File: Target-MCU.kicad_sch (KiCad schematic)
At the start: 19 parts, among them Q6 DMG1012UW-7, SW5 16V 50mA, U4 CH32V003F4P6

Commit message: Update parts
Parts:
- removed SW5: 16V 50mA, Tiny_Scarab:SW_Tactile_SPST_NO_Straight_ALPSALPINE_SKRP, symbol Tiny_Scarab:SW_SKRPASE010
- added SW5: 12V 50mA, Tiny_Scarab:SW_Tactile_SPST_NO_Straight_Korean-Hroparts_K2-1109SP-I4SA-04, symbol Tiny_Scarab:SW_K2-1109SP-I4SA-04
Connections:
- net GND: now also SW5.3, SW5.4
- net at C41.1, R25.2, R26.1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: now also SW5.1, SW5.2
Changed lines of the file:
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@@
     (effects (font (size 1.27 1.27)) (justify right))
-  )
-  (symbol (lib_id "Tiny_Scarab:SW_SKRPASE010") (at 191.77 54.61 270) (unit 1)
-    (in_bom yes) (on_board yes) (dnp no)
-    (property "Reference" "SW5" (at 193.04 53.34 90)
-      (effects (font (size 1.27 1.27)) (justify left))
-    )
-    (property "Value" "16V 50mA" (at 217.17 54.61 0)
-      (effects (font (size 1.27 1.27)) hide)
-    )
-    (property "Footprint" "Tiny_Scarab:SW_Tactile_SPST_NO_Straight_ALPSALPINE_SKRP" (at 219.71 54.61 0)
-      (effects (font (size 1.27 1.27)) hide)
-    )
-    (property "Datasheet" "https://www.farnell.com/datasheets/2864500.pdf" (at 214.63 54.61 0)
-      (effects (font (size 1.27 1.27)) hide)
-    )
-    (property "Manufacturer" "ALPSALPINE" (at 212.09 54.61 0)
-      (effects (font (size 1.27 1.27)) hide)
-    )
-    (property "MPN" "SKRPASE010" (at 209.55 54.61 0)
-      (effects (font (size 1.27 1.27)) hide)
-    )
-    (property "JLCPCB Part #" "C470427" (at 207.01 54.61 0)
-      (effects (font (size 1.27 1.27)) hide)
-    )
-    (property "DigiKey" "4809-SKRPADE010TR-ND" (at 204.47 54.61 0)
-      (effects (font (size 1.27 1.27)) hide)
-    )
-    (property "Farnell" "3261826" (at 201.93 54.61 0)
-      (effects (font (size 1.27 1.27)) hide)
-    )
-    (property "Mouser" "688-SKRPASE010" (at 199.39 54.61 0)
-      (effects (font (size 1.27 1.27)) hide)
-    )
-    (pin "4")
-    (pin "3")
-    (pin "2")
-    (pin "1")
-    (instances
-      (project "tiny-scarab"
-        (path "/156c5422-ee07-49a4-8263-a2dbd26b90bd/d0c4b0c3-1e7e-4a4c-add3-8d4a3a10843d"
-          (reference "SW5") (unit 1)
-        )
-      )
-    )
   )
   (symbol (lib_id "Tiny_Scarab:IC_CH32V003F4P6") (at 118.11 57.15 0) (unit 1)
@@
         )
       )
+    )
+  )
+  (symbol (lib_id "Tiny_Scarab:SW_K2-1109SP-I4SA-04") (at 191.77 54.61 270) (unit 1)
+    (in_bom yes) (on_board yes) (dnp no)
+    (property "Reference" "SW5" (at 193.04 53.34 90)
+      (effects (font (size 1.27 1.27)) (justify left))
+    )
+    (property "Value" "12V 50mA" (at 217.17 54.61 0)
+      (effects (font (size 1.27 1.27)) hide)
+    )
+    (property "Footprint" "Tiny_Scarab:SW_Tactile_SPST_NO_Straight_Korean-Hroparts_K2-1109SP-I4SA-04" (at 219.71 54.61 0)
+      (effects (font (size 1.27 1.27)) hide)
+    )
+    (property "Datasheet" "" (at 214.63 54.61 0)
+      (effects (font (size 1.27 1.27)) hide)
+    )
+    (property "Manufacturer" "Korean Hroparts Elec" (at 212.09 54.61 0)
+      (effects (font (size 1.27 1.27)) hide)
+    )
+    (property "MPN" "K2-1109SP-I4SA-04" (at 209.55 54.61 0)
+      (effects (font (size 1.27 1.27)) hide)
+    )
+    (property "JLCPCB Part #" "C146695" (at 207.01 54.61 0)
+      (effects (font (size 1.27 1.27)) hide)
+    )
+    (property "DigiKey" "" (at 204.47 54.61 0)
+      (effects (font (size 1.27 1.27)) hide)
+    )
+    (property "Farnell" "" (at 201.93 54.61 0)
+      (effects (font (size 1.27 1.27)) hide)
+    )
+    (property "Mouser" "" (at 199.39 54.61 0)
+      (effects (font (size 1.27 1.27)) hide)
+    )
+    (pin "2")
+    (pin "4")
+    (pin "1")
+    (pin "3")
+    (instances
+      (project "tiny-scarab"
+        (path "/156c5422-ee07-49a4-8263-a2dbd26b90bd/d0c4b0c3-1e7e-4a4c-add3-8d4a3a10843d"
+          (reference "SW5") (unit 1)
+        )
+      )

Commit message: Work on BOM
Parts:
- LED5: JLCPCB Part # (none) -> C7115899
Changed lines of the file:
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@@
       (effects (font (size 1.27 1.27)) hide)
     )
-    (property "JLCPCB Part #" "" (at 25.4 88.9 0)
+    (property "JLCPCB Part #" "C7115899" (at 25.4 88.9 0)
       (effects (font (size 1.27 1.27)) hide)
     )

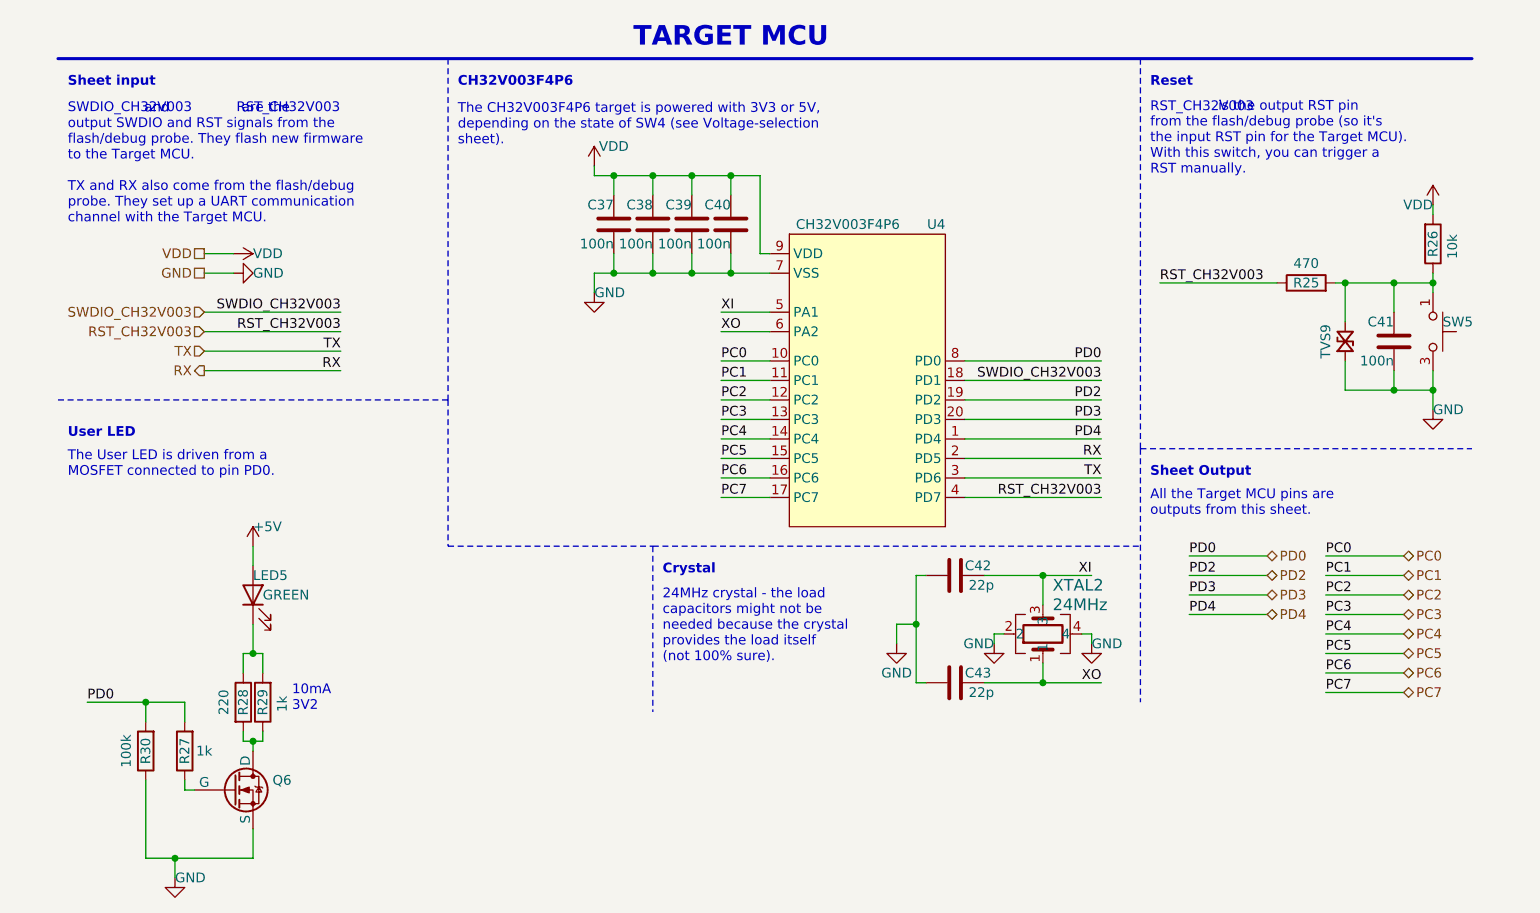
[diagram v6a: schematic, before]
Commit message: Modify resistors for LEDs
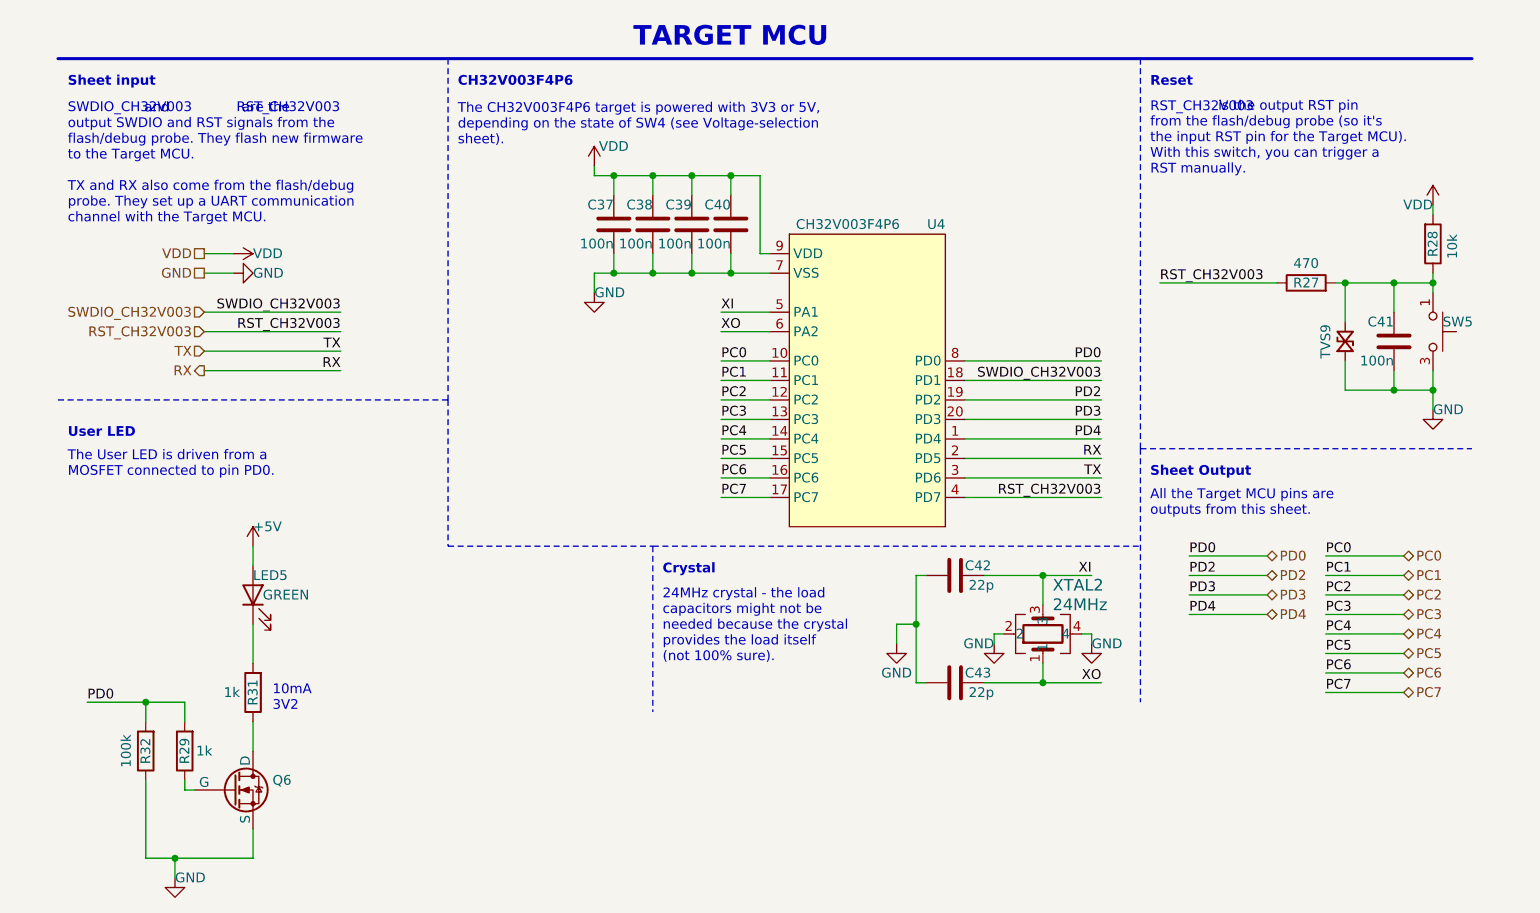
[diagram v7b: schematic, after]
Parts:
- removed R28: 220, Resistor_SMD:R_0402_1005Metric_Pad0.72x0.64mm_HandSolder, symbol Device:R
- renumbered R25 to R27, R26 to R28, R27 to R29, R29 to R31, R30 to R32
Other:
- moved on the sheet: R31
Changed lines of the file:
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@@
     (comment 2 "https://github.com/Embeetle/tiny-scarab")
   )
-  (junction (at 38.1 96.52) (diameter 0) (color 0 0 0 0)
-  )
   (junction (at 85.09 46.99) (diameter 0) (color 0 0 0 0)
   )
@@
   (junction (at 27.94 123.19) (diameter 0) (color 0 0 0 0)
   )
-  (junction (at 38.1 107.95) (diameter 0) (color 0 0 0 0)
-  )
   (junction (at 90.17 46.99) (diameter 0) (color 0 0 0 0)
   )
@@
   )
   (wire (pts (xy 124.46 100.33) (xy 124.46 92.71))
-    (stroke (width 0) (type default))
-  )
-  (wire (pts (xy 39.37 106.68) (xy 39.37 107.95))
     (stroke (width 0) (type default))
   )
@@
     (stroke (width 0) (type default))
   )
-  (wire (pts (xy 36.83 107.95) (xy 36.83 106.68))
-    (stroke (width 0) (type default))
-  )
-  (wire (pts (xy 38.1 92.71) (xy 38.1 96.52))
-    (stroke (width 0) (type default))
-  )
   (wire (pts (xy 130.81 73.66) (xy 148.59 73.66))
     (stroke (width 0) (type default))
@@
     (stroke (width 0) (type default))
   )
-  (wire (pts (xy 38.1 109.22) (xy 38.1 107.95))
+  (wire (pts (xy 38.1 105.41) (xy 38.1 109.22))
     (stroke (width 0) (type default))
   )
@@
     (stroke (width 0) (type default))
   )
-  (wire (pts (xy 38.1 107.95) (xy 36.83 107.95))
-    (stroke (width 0) (type default))
-  )
   (wire (pts (xy 177.8 88.9) (xy 187.96 88.9))
     (stroke (width 0) (type default))
@@
     (stroke (width 0) (type dash))
   )
-  (wire (pts (xy 39.37 107.95) (xy 38.1 107.95))
-    (stroke (width 0) (type default))
-  )
   (wire (pts (xy 186.69 59.69) (xy 186.69 62.23))
     (stroke (width 0) (type default))
@@
     (stroke (width 0) (type default))
   )
-  (wire (pts (xy 38.1 96.52) (xy 39.37 96.52))
-    (stroke (width 0) (type default))
-  )
   (wire (pts (xy 99.06 71.12) (xy 105.41 71.12))
     (stroke (width 0) (type default))
@@
     (stroke (width 0) (type default))
   )
-  (wire (pts (xy 39.37 96.52) (xy 39.37 99.06))
+  (wire (pts (xy 38.1 92.71) (xy 38.1 97.79))
     (stroke (width 0) (type default))
   )
@@
     (stroke (width 0) (type default))
   )
-  (wire (pts (xy 36.83 99.06) (xy 36.83 96.52))
-    (stroke (width 0) (type default))
-  )
   (wire (pts (xy 146.05 93.98) (xy 147.32 93.98))
     (stroke (width 0) (type default))
@@
   )
   (wire (pts (xy 177.8 93.98) (xy 187.96 93.98))
-    (stroke (width 0) (type default))
-  )
-  (wire (pts (xy 36.83 96.52) (xy 38.1 96.52))
     (stroke (width 0) (type default))
   )
@@
     (effects (font (size 1.27 1.27)) (justify left bottom))
   )
-  (text "10mA\n3V2" (at 43.18 104.14 0)
+  (text "10mA\n3V2" (at 40.64 104.14 0)
     (effects (font (size 1.27 1.27)) (justify left bottom))
   )
@@
   (symbol (lib_id "Device:R") (at 191.77 43.18 0) (mirror x) (unit 1)
     (in_bom yes) (on_board yes) (dnp no)
-    (property "Reference" "R26" (at 191.77 43.18 90)
+    (property "Reference" "R28" (at 191.77 43.18 90)
       (effects (font (size 1.27 1.27)))
     )
@@
       (project "tiny-scarab"
         (path "/156c5422-ee07-49a4-8263-a2dbd26b90bd/d0c4b0c3-1e7e-4a4c-add3-8d4a3a10843d"
-          (reference "R26") (unit 1)
+          (reference "R28") (unit 1)
         )
       )
@@
   (symbol (lib_id "Device:R") (at 29.21 109.22 180) (unit 1)
     (in_bom yes) (on_board yes) (dnp no)
-    (property "Reference" "R27" (at 29.21 109.22 90)
+    (property "Reference" "R29" (at 29.21 109.22 90)
       (effects (font (size 1.27 1.27)))
     )
@@
       (project "tiny-scarab"
         (path "/156c5422-ee07-49a4-8263-a2dbd26b90bd/d0c4b0c3-1e7e-4a4c-add3-8d4a3a10843d"
-          (reference "R27") (unit 1)
+          (reference "R29") (unit 1)
         )
       )
@@
     )
   )
-  (symbol (lib_id "Device:R") (at 36.83 102.87 0) (unit 1)
-    (in_bom yes) (on_board yes) (dnp no)
-    (property "Reference" "R28" (at 36.83 102.87 90)
-      (effects (font (size 1.27 1.27)))
-    )
-    (property "Value" "220" (at 34.29 102.87 90)
-      (effects (font (size 1.27 1.27)))
-    )
-    (property "Footprint" "Resistor_SMD:R_0402_1005Metric_Pad0.72x0.64mm_HandSolder" (at 35.052 102.87 90)
-      (effects (font (size 1.27 1.27)) hide)
-    )
-    (property "Datasheet" "~" (at 36.83 102.87 0)
-      (effects (font (size 1.27 1.27)) hide)
-    )
-    (property "Manufacturer" "UNI-ROYAL(Uniroyal Elec)" (at 36.83 102.87 90)
-      (effects (font (size 1.27 1.27)) hide)
-    )
-    (property "MPN" "0402WGF2200TCE" (at 36.83 102.87 90)
-      (effects (font (size 1.27 1.27)) hide)
-    )
-    (property "JLCPCB Part #" "C25091" (at 36.83 102.87 90)
-      (effects (font (size 1.27 1.27)) hide)
-    )
-    (pin "2")
-    (pin "1")
-    (instances
-      (project "tiny-scarab"
-        (path "/156c5422-ee07-49a4-8263-a2dbd26b90bd/d0c4b0c3-1e7e-4a4c-add3-8d4a3a10843d"
-          (reference "R28") (unit 1)
-        )
-      )
-    )
-  )
   (symbol (lib_id "Device:R") (at 175.26 48.26 90) (unit 1)
     (in_bom yes) (on_board yes) (dnp no)
-    (property "Reference" "R25" (at 175.26 48.26 90)
+    (property "Reference" "R27" (at 175.26 48.26 90)
       (effects (font (size 1.27 1.27)))
     )
@@
       (project "tiny-scarab"
         (path "/156c5422-ee07-49a4-8263-a2dbd26b90bd/d0c4b0c3-1e7e-4a4c-add3-8d4a3a10843d"
-          (reference "R25") (unit 1)
+          (reference "R27") (unit 1)
         )
       )
@@
   (symbol (lib_id "Device:R") (at 24.13 109.22 180) (unit 1)
     (in_bom yes) (on_board yes) (dnp no)
-    (property "Reference" "R30" (at 24.13 109.22 90)
+    (property "Reference" "R32" (at 24.13 109.22 90)
       (effects (font (size 1.27 1.27)))
     )
@@
       (project "tiny-scarab"
         (path "/156c5422-ee07-49a4-8263-a2dbd26b90bd/d0c4b0c3-1e7e-4a4c-add3-8d4a3a10843d"
-          (reference "R30") (unit 1)
+          (reference "R32") (unit 1)
         )
       )
@@
     )
   )
-  (symbol (lib_id "Device:R") (at 39.37 102.87 180) (unit 1)
-    (in_bom yes) (on_board yes) (dnp no)
-    (property "Reference" "R29" (at 39.37 102.87 90)
+  (symbol (lib_id "Device:R") (at 38.1 101.6 180) (unit 1)
+    (in_bom yes) (on_board yes) (dnp no)
+    (property "Reference" "R31" (at 38.1 101.6 90)
       (effects (font (size 1.27 1.27)))
     )
-    (property "Value" "1k" (at 41.91 104.14 90)
+    (property "Value" "1k" (at 34.29 101.6 0)
       (effects (font (size 1.27 1.27)) (justify right))
     )
-    (property "Footprint" "Resistor_SMD:R_0402_1005Metric_Pad0.72x0.64mm_HandSolder" (at 41.148 102.87 90)
-      (effects (font (size 1.27 1.27)) hide)
-    )
-    (property "Datasheet" "~" (at 39.37 102.87 0)
-      (effects (font (size 1.27 1.27)) hide)
-    )
-    (property "Manufacturer" "UNI-ROYAL(Uniroyal Elec)" (at 39.37 102.87 0)
-      (effects (font (size 1.27 1.27)) hide)
-    )
-    (property "MPN" "0402WGF1001TCE" (at 39.37 102.87 90)
-      (effects (font (size 1.27 1.27)) hide)
-    )
-    (property "JLCPCB Part #" "C11702" (at 39.37 102.87 90)
-      (effects (font (size 1.27 1.27)) hide)
-    )
-    (pin "2")
-    (pin "1")
-    (instances
-      (project "tiny-scarab"
-        (path "/156c5422-ee07-49a4-8263-a2dbd26b90bd/d0c4b0c3-1e7e-4a4c-add3-8d4a3a10843d"
-          (reference "R29") (unit 1)
-        )
-      )
+    (property "Footprint" "Resistor_SMD:R_0402_1005Metric_Pad0.72x0.64mm_HandSolder" (at 39.878 101.6 90)
+      (effects (font (size 1.27 1.27)) hide)
+    )
+    (property "Datasheet" "~" (at 38.1 101.6 0)
+      (effects (font (size 1.27 1.27)) hide)
+    )
+    (property "Manufacturer" "UNI-ROYAL(Uniroyal Elec)" (at 38.1 101.6 0)
+      (effects (font (size 1.27 1.27)) hide)
+    )
+    (property "MPN" "0402WGF1001TCE" (at 38.1 101.6 90)
+      (effects (font (size 1.27 1.27)) hide)
+    )
+    (property "JLCPCB Part #" "C11702" (at 38.1 101.6 90)
+      (effects (font (size 1.27 1.27)) hide)
+    )
+    (pin "2")
+    (pin "1")
+    (instances
+      (project "tiny-scarab"
+        (path "/156c5422-ee07-49a4-8263-a2dbd26b90bd/d0c4b0c3-1e7e-4a4c-add3-8d4a3a10843d"
+          (reference "R31") (unit 1)
+        )
+      )
